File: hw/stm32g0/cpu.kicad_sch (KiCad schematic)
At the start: 20 parts, among them J201 Conn_01x06, J202 Conn_01x04, J203 Conn_01x03, U201 STM32G030K8Tx, U202 74AHCT125, U203 CAT24C256

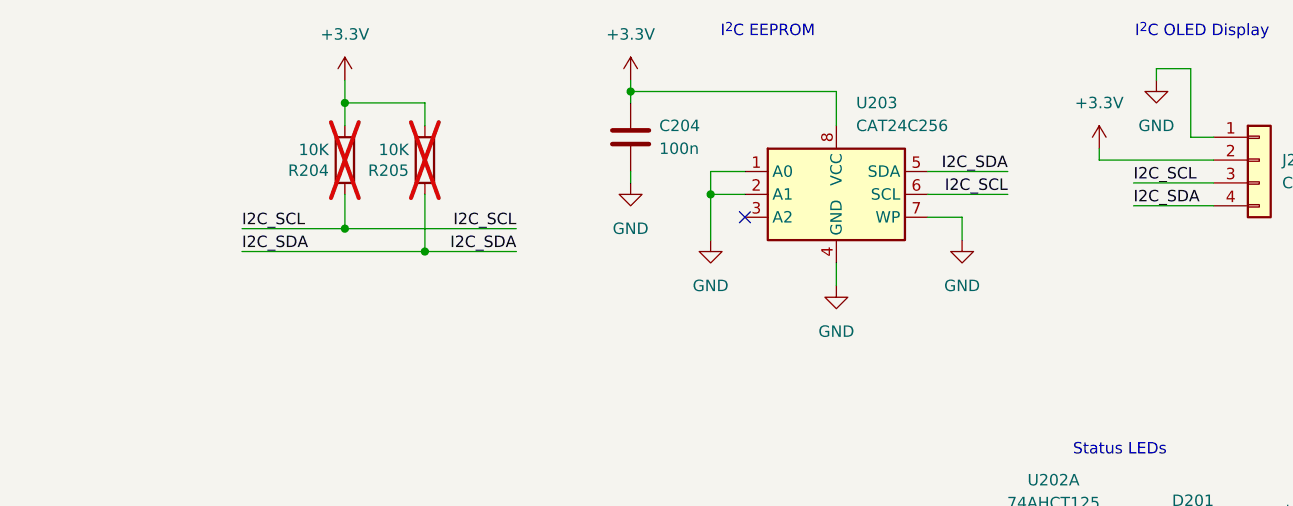
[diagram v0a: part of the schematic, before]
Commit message: chore(hw): minor layout and schematic improvements
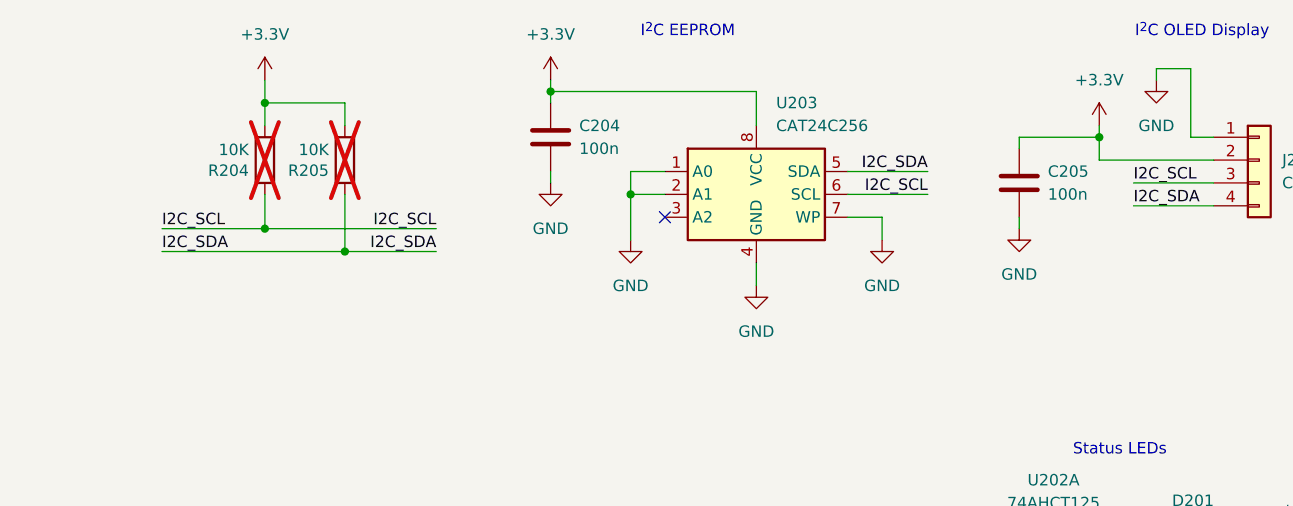
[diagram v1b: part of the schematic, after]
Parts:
- added C205: 100n, Capacitor_SMD:C_0805_2012Metric_Pad1.18x1.45mm_HandSolder, symbol Device:C
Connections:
- net +3.3V: now also C205.1
- net GND: now also C205.2
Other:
- moved on the sheet: C204, R204, R205, U203

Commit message: chore(hw): update title blocks
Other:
- company: (none) -> Stefan Misik
- title: (none) -> STM32G0 LED Controller
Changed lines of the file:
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@@
 	(generator_version "8.0")
 	(paper "A4")
+	(title_block
+		(title "STM32G0 LED Controller")
+		(date "2024-06-29")
+		(company "Stefan Misik")
+		(comment 1 "www.stefanmisik.com")
+	)
 	(junction
 		(at 199.39 153.67)

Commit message: chore(hw): tune the layout
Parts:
- R204, R205: now fitted
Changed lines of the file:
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@@
 		(in_bom yes)
 		(on_board yes)
-		(dnp yes)
+		(dnp no)
 		(property "Reference" "R205"
 			(at 163.322 34.1884 0)
@@
 		(in_bom yes)
 		(on_board yes)
-		(dnp yes)
+		(dnp no)
 		(property "Reference" "R204"
 			(at 154.432 34.1884 0)

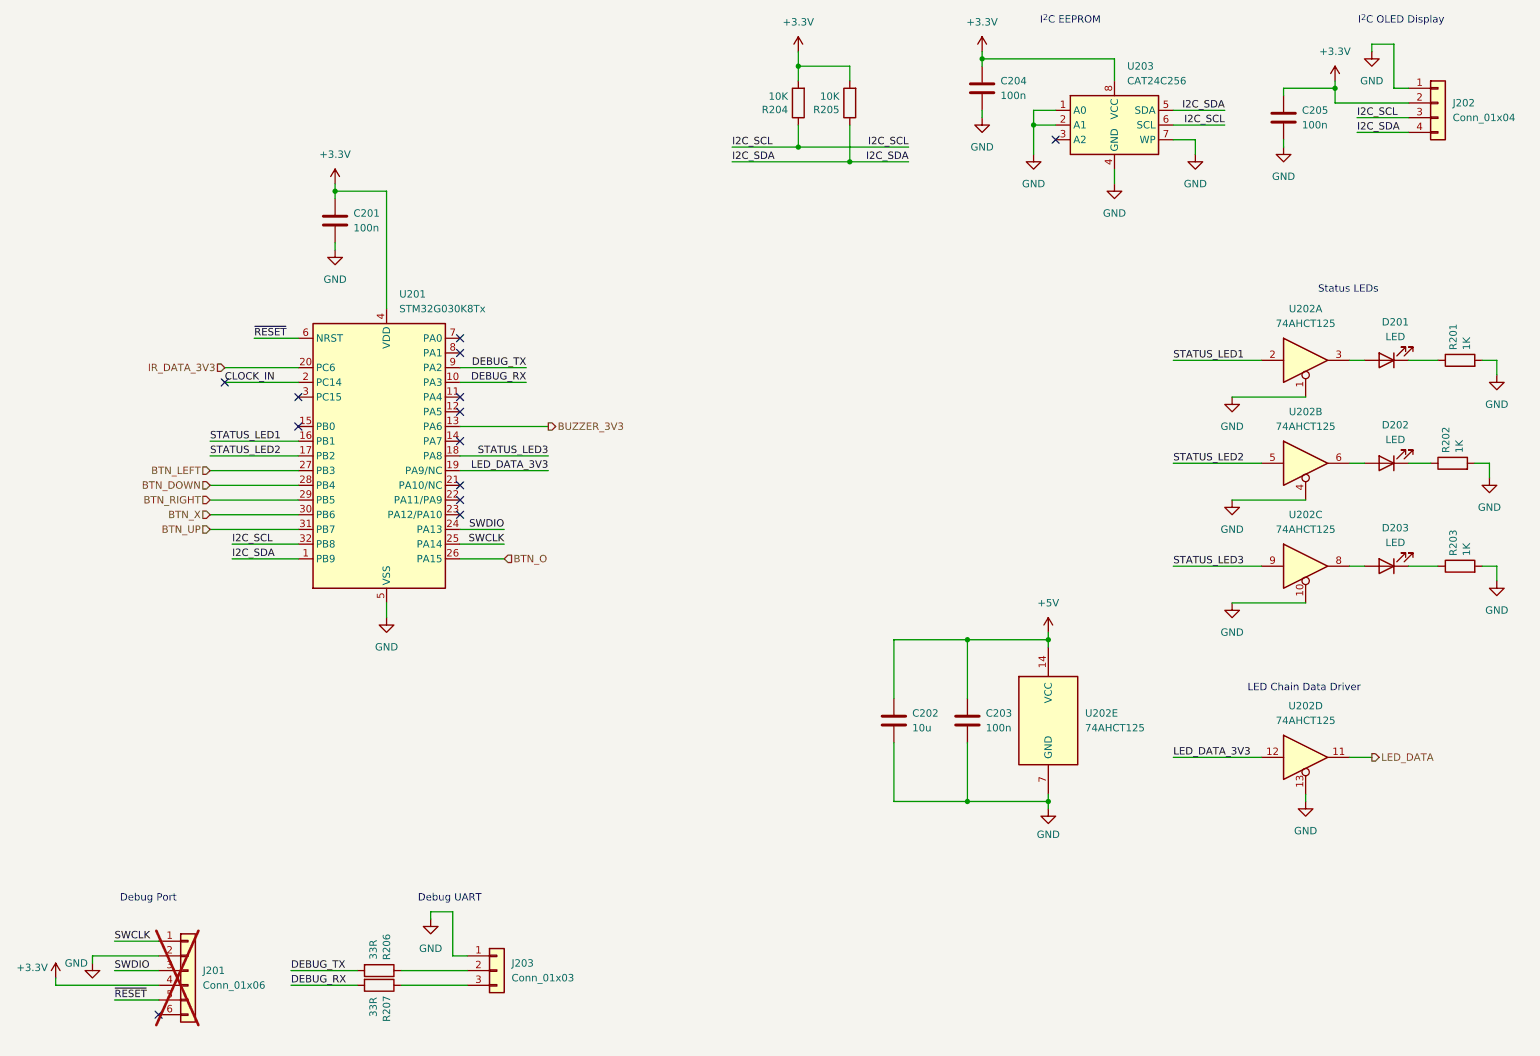
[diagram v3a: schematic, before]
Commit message: chore(hw): add ESD protection diodes
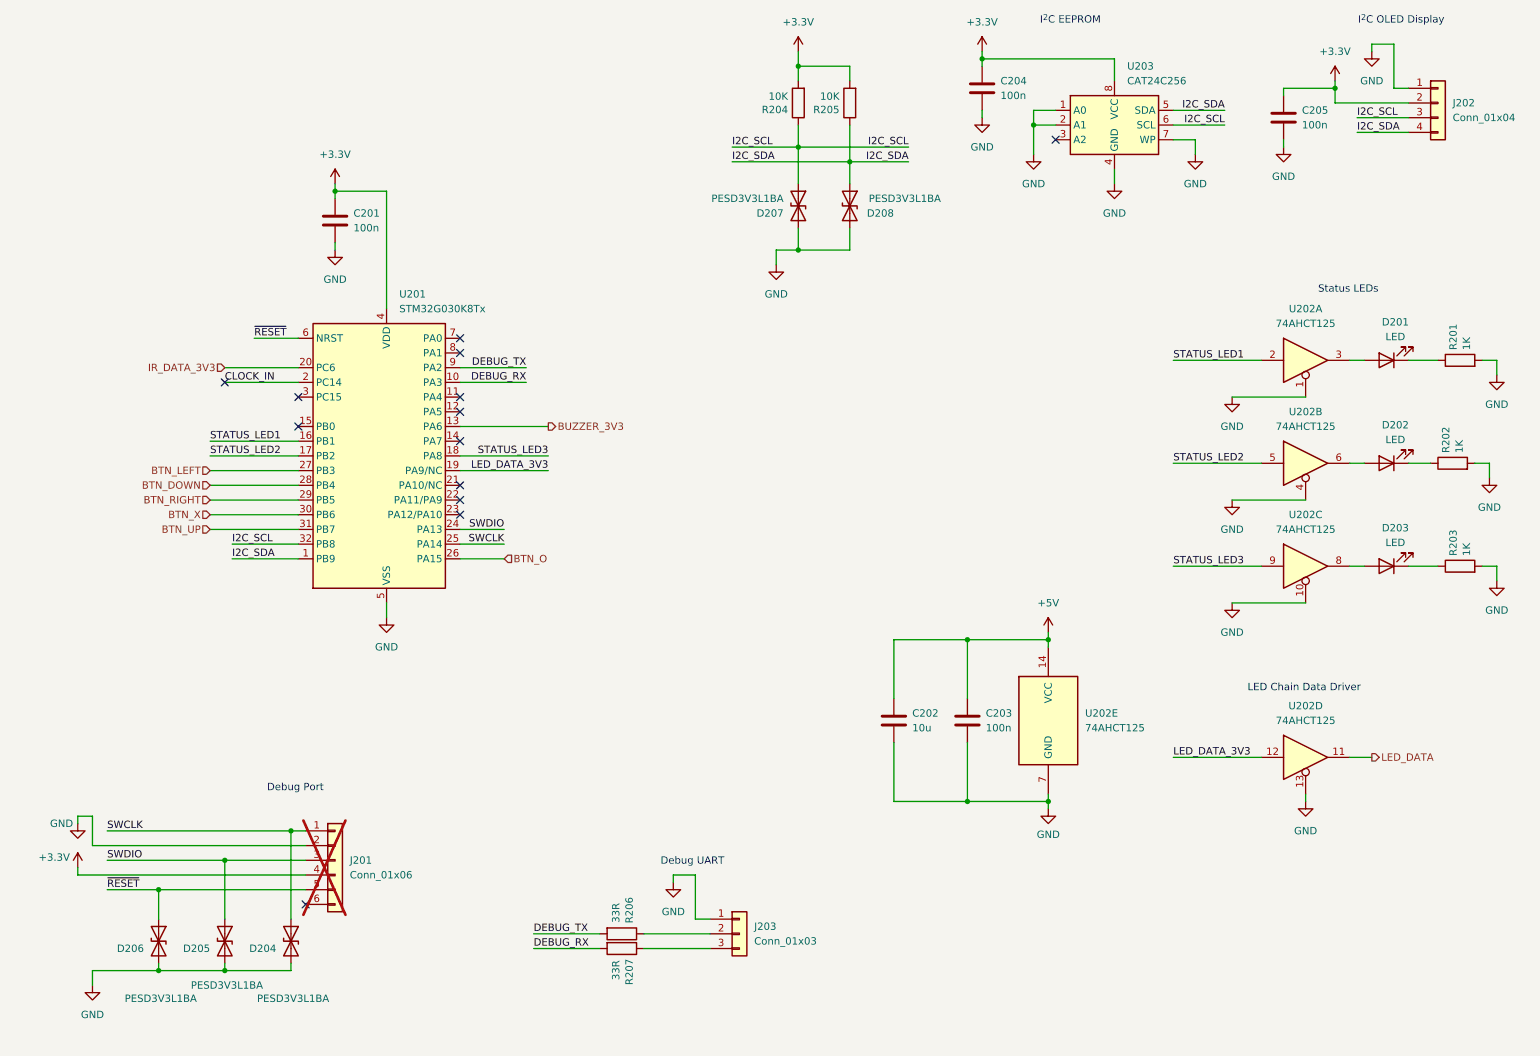
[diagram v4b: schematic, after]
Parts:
- added D204, D205, D206, D207, D208: PESD3V3L1BA, Diode_SMD:D_SOD-323_HandSoldering, symbol Device:D_TVS
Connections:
- net GND: now also D204.2 (A2), D205.2 (A2), D206.2 (A2), D207.2 (A2), D208.2 (A2)
- net I2C_SCL: now also D207.1 (A1)
- net I2C_SDA: now also D208.1 (A1)
- net SWCLK: now also D204.1 (A1)
- net SWDIO: now also D205.1 (A1)
- net ~{RESET}: now also D206.1 (A1)
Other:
- moved on the sheet: J201, J203, R206, R207

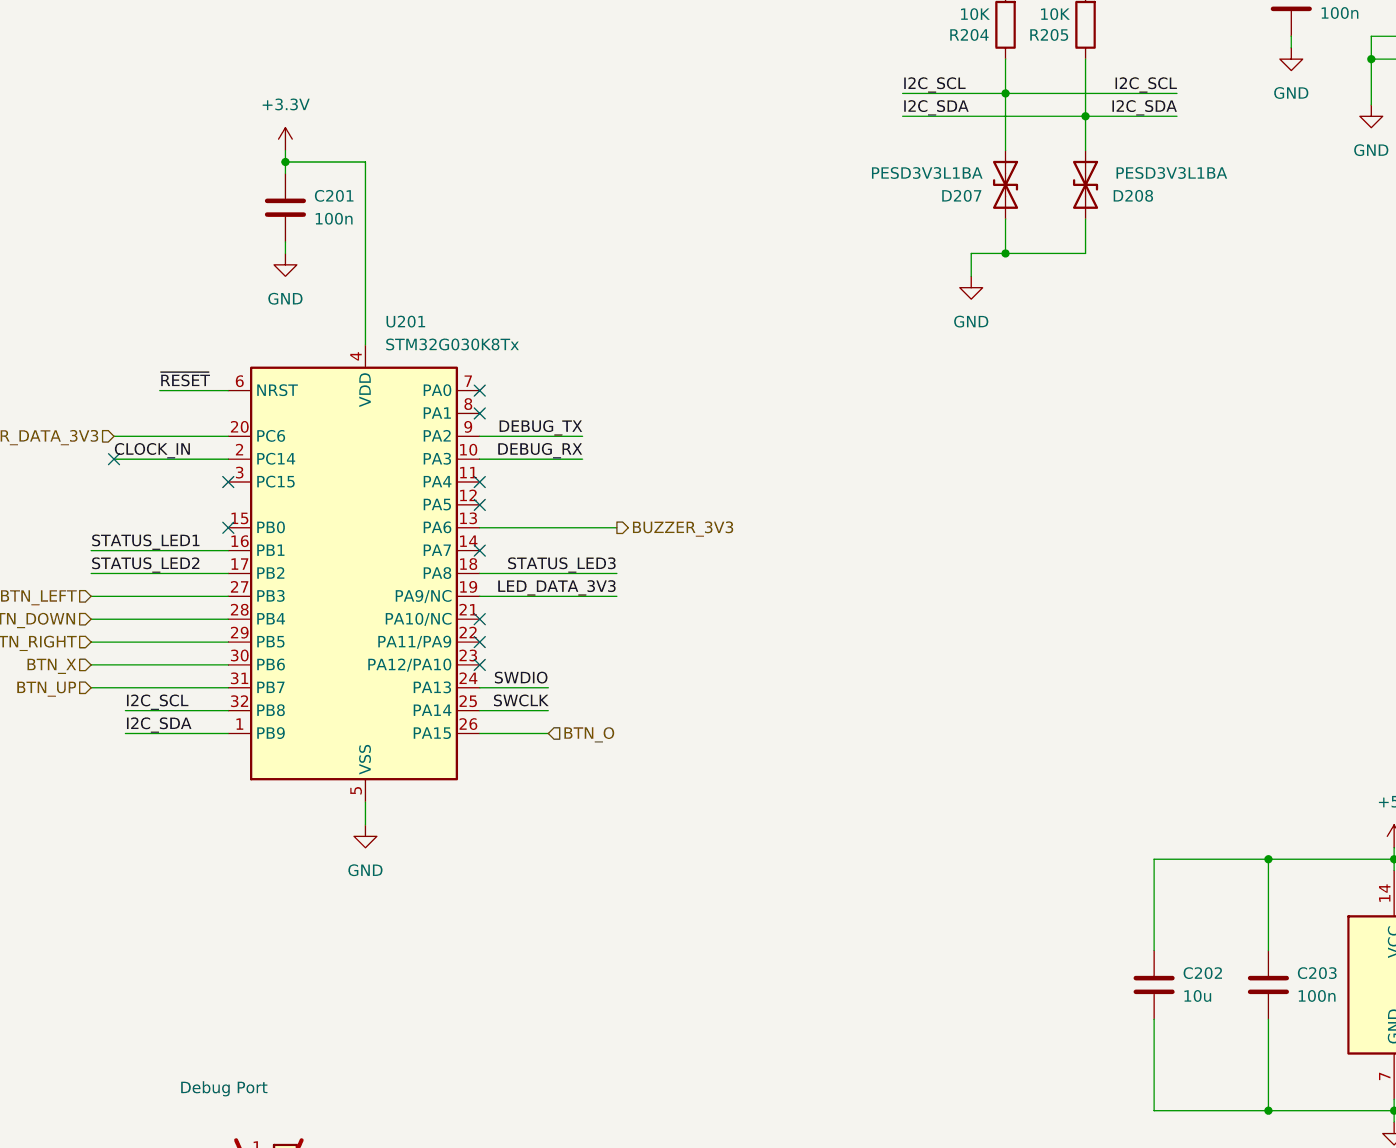
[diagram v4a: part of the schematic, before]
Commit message: chore(hw): increase CPU decoupling
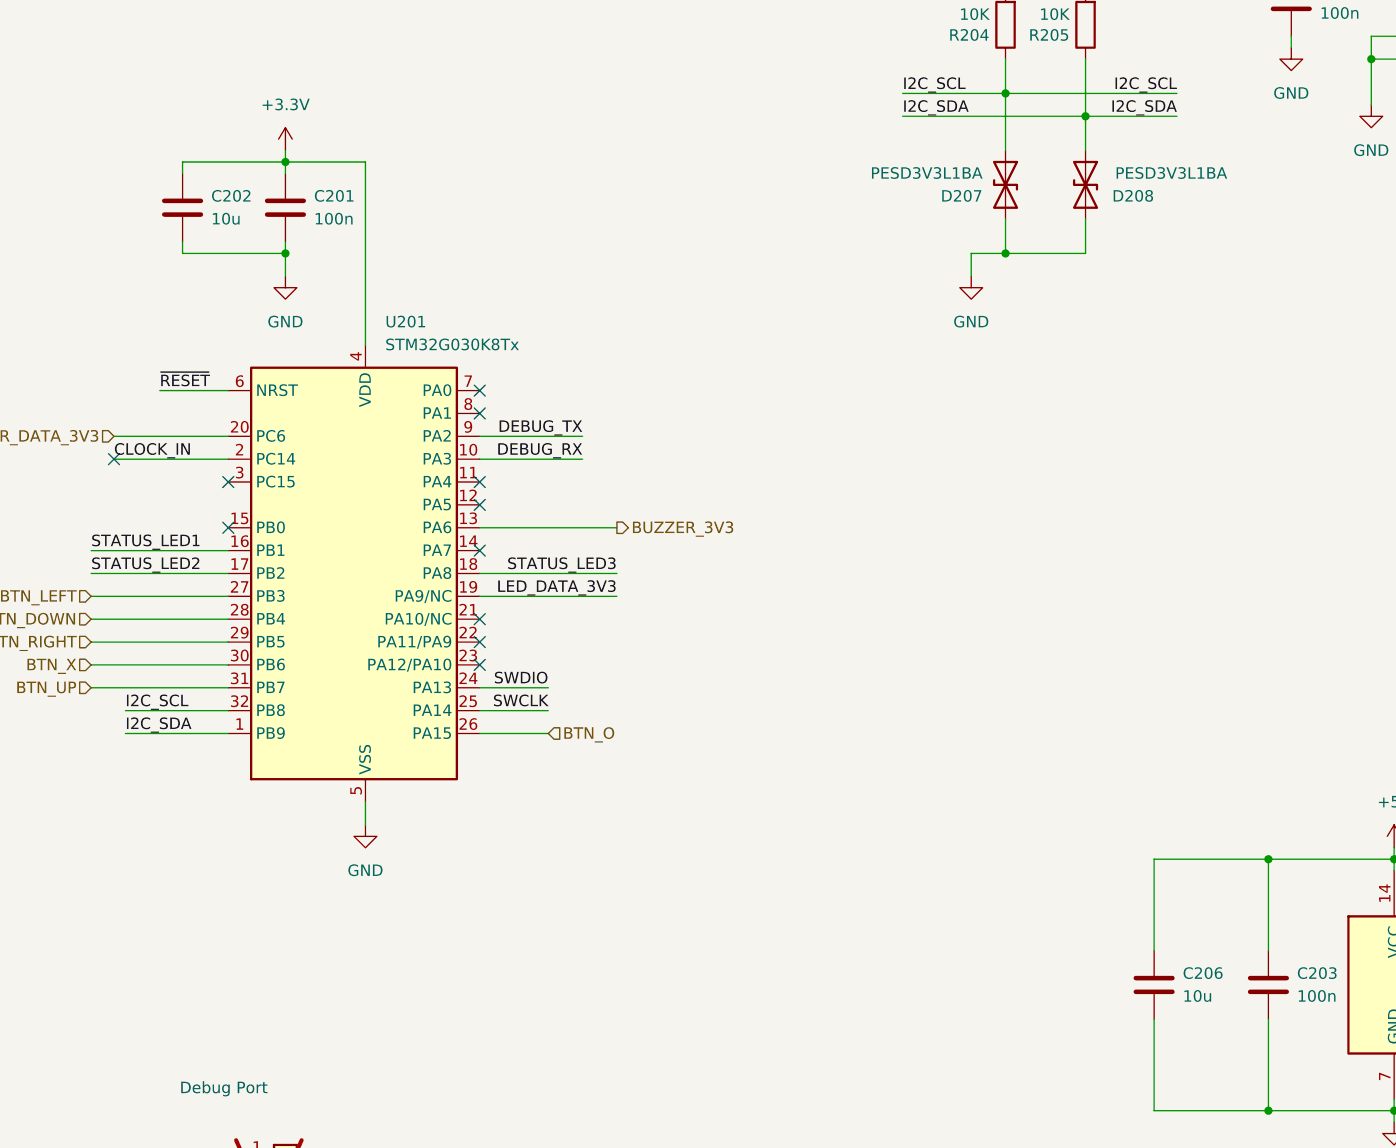
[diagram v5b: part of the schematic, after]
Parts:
- added C206: 10u, Capacitor_SMD:C_1206_3216Metric_Pad1.33x1.80mm_HandSolder, symbol Device:C
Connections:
- net +3.3V: now also C202.1
- net +5V: now also C206.1; no longer C202.1
- net GND: now also C206.2
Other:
- moved on the sheet: C202
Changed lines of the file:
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@@
 	)
 	(junction
+		(at 76.2 58.42)
+		(diameter 0)
+		(color 0 0 0 0)
+	)
+	(junction
 		(at 196.85 36.83)
 		(diameter 0)
@@
 	(wire
 		(pts
+			(xy 64.77 58.42) (xy 76.2 58.42)
+		)
+		(stroke
+			(width 0)
+			(type default)
+		)
+	)
+	(wire
+		(pts
 			(xy 259.08 30.48) (xy 261.62 30.48)
 		)
@@
 	(wire
 		(pts
+			(xy 64.77 57.15) (xy 64.77 58.42)
+		)
+		(stroke
+			(width 0)
+			(type default)
+		)
+	)
+	(wire
+		(pts
 			(xy 187.96 25.4) (xy 187.96 24.13)
 		)
@@
 	(wire
 		(pts
+			(xy 76.2 48.26) (xy 64.77 48.26)
+		)
+		(stroke
+			(width 0)
+			(type default)
+		)
+	)
+	(wire
+		(pts
 			(xy 54.61 101.6) (xy 69.85 101.6)
 		)
@@
 	(wire
 		(pts
+			(xy 76.2 60.96) (xy 76.2 58.42)
+		)
+		(stroke
+			(width 0)
+			(type default)
+		)
+	)
+	(wire
+		(pts
 			(xy 261.62 38.1) (xy 252.73 38.1)
 		)
@@
 	(wire
 		(pts
+			(xy 64.77 48.26) (xy 64.77 49.53)
+		)
+		(stroke
+			(width 0)
+			(type default)
+		)
+	)
+	(wire
+		(pts
 			(xy 185.42 143.51) (xy 185.42 153.67)
 		)
@@
 	(symbol
 		(lib_id "power:GND")
-		(at 76.2 58.42 0)
+		(at 76.2 60.96 0)
 		(unit 1)
 		(exclude_from_sim no)
@@
 		(fields_autoplaced yes)
 		(property "Reference" "#PWR0206"
-			(at 76.2 64.77 0)
+			(at 76.2 67.31 0)
 			(effects
 				(font
@@
 		)
 		(property "Value" "GND"
-			(at 76.2 63.5 0)
+			(at 76.2 66.04 0)
 			(effects
 				(font
@@
 		)
 		(property "Footprint" ""
-			(at 76.2 58.42 0)
+			(at 76.2 60.96 0)
 			(effects
 				(font
@@
 		)
 		(property "Datasheet" ""
-			(at 76.2 58.42 0)
+			(at 76.2 60.96 0)
 			(effects
 				(font
@@
 		)
 		(property "Description" "Power symbol creates a global label with name \"GND\" , ground"
-			(at 76.2 58.42 0)
+			(at 76.2 60.96 0)
 			(effects
 				(font
@@
 	)
 	(symbol
+		(lib_id "Device:C")
+		(at 172.72 139.7 0)
+		(unit 1)
+		(exclude_from_sim no)
+		(in_bom yes)
+		(on_board yes)
+		(dnp no)
+		(fields_autoplaced yes)
+		(property "Reference" "C206"
+			(at 175.895 138.43 0)
+			(effects
+				(font
+					(size 1.27 1.27)
+				)
+				(justify left)
+			)
+		)
+		(property "Value" "10u"
+			(at 175.895 140.97 0)
+			(effects
+				(font
+					(size 1.27 1.27)
+				)
+				(justify left)
+			)
+		)
+		(property "Footprint" "Capacitor_SMD:C_1206_3216Metric_Pad1.33x1.80mm_HandSolder"
+			(at 173.6852 143.51 0)
+			(effects
+				(font
+					(size 1.27 1.27)
+				)
+				(hide yes)
+			)
+		)
+		(property "Datasheet" "~"
+			(at 172.72 139.7 0)
+			(effects
+				(font
+					(size 1.27 1.27)
+				)
+				(hide yes)
+			)
+		)
+		(property "Description" "Unpolarized capacitor"
+			(at 172.72 139.7 0)
+			(effects
+				(font
+					(size 1.27 1.27)
+				)
+				(hide yes)
+			)
+		)
+		(pin "2"
+		)
+		(pin "1"
+		)
+		(instances
+			(project "stm32g0"
+				(path "/fc4ba96f-a9f8-4f1a-a9c5-2b16679a6770/32819f2b-3e26-4dff-931e-dc604d389a45"
+					(reference "C206")
+					(unit 1)
+				)
+			)
+		)
+	)
+	(symbol
 		(lib_id "74xx:74AHCT125")
 		(at 243.84 146.05 0)
@@
 	(symbol
 		(lib_id "Device:C")
-		(at 172.72 139.7 0)
+		(at 64.77 53.34 0)
 		(unit 1)
 		(exclude_from_sim no)
@@
 		(fields_autoplaced yes)
 		(property "Reference" "C202"
-			(at 175.895 138.43 0)
+			(at 67.945 52.07 0)
 			(effects
 				(font
@@
 		)
 		(property "Value" "10u"
-			(at 175.895 140.97 0)
+			(at 67.945 54.61 0)
 			(effects
 				(font
@@
 		)
 		(property "Footprint" "Capacitor_SMD:C_1206_3216Metric_Pad1.33x1.80mm_HandSolder"
-			(at 173.6852 143.51 0)
+			(at 65.7352 57.15 0)
 			(effects
 				(font
@@
 		)
 		(property "Datasheet" "~"
-			(at 172.72 139.7 0)
+			(at 64.77 53.34 0)
 			(effects
 				(font
@@
 		)
 		(property "Description" "Unpolarized capacitor"
-			(at 172.72 139.7 0)
+			(at 64.77 53.34 0)
 			(effects
 				(font
